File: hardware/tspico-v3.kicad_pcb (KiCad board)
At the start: 4 copper layers, 130 x 56 mm, 147 parts, among them J1 USB-C, J2 microSD, J3 OLED 1.27in 128x96, J4 3.5mm stereo, J5 Joystick, P1 TS2068_Edge, SW1 TS Reset, SW2 NMI, SW3 RUN, SW4 BOOTSEL, U1 74LVC245APW, U15 XL9555, U2 74LVC245APW, U20 RP2350B, U21 GD25Q128ESIGR, U22 APS6404L-3SQR-SN, U3 74LVC245APW, U30 TLV1117LV33, U31 TLV1117LV33, U4 74LVC245APW, U40 ESP32-C3-WROOM-02-N4, U50 MCP6002, U6 74LVC32APW, U7 74LVC06AD, Y1 12MHz

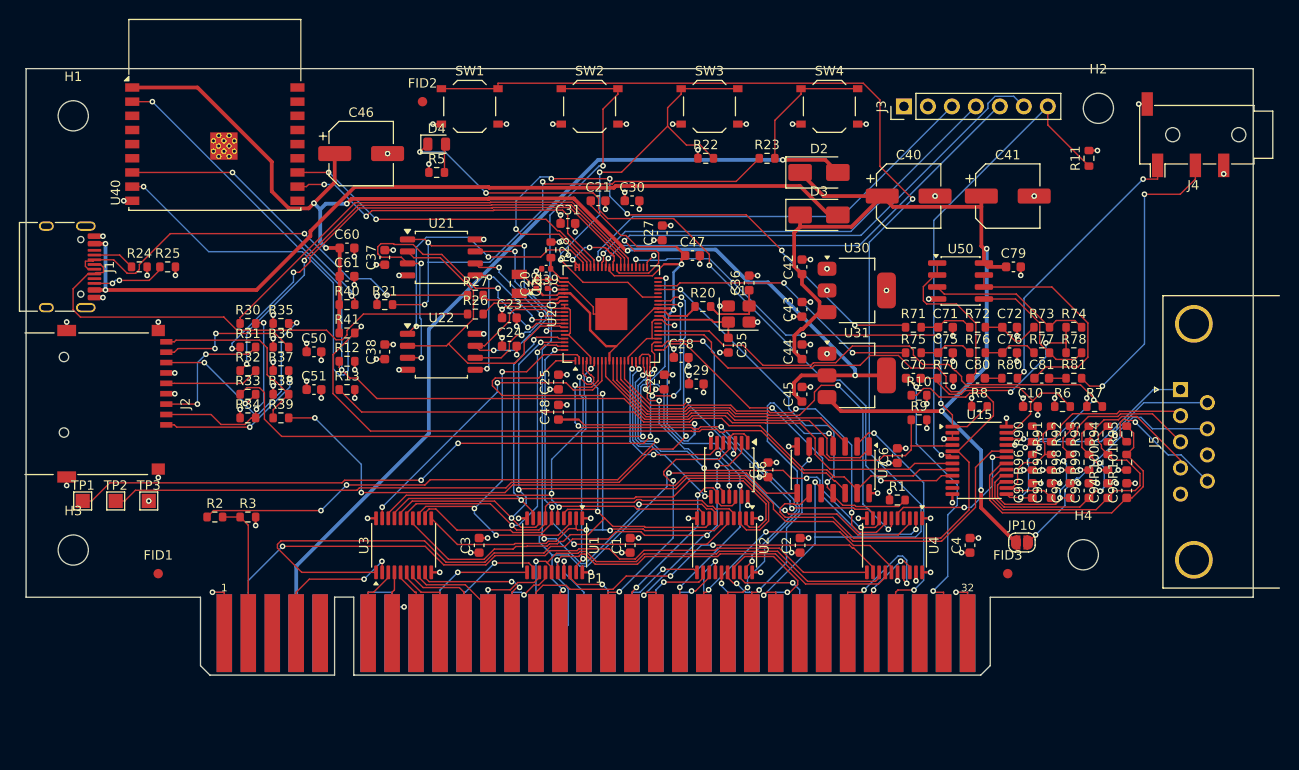
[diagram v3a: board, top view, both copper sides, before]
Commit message: Plain address bytes in hardware; DVDD spine and bottom-row fan pre-routed
U1 delivers A0-A7 and U2 A8-A15 on MD0-MD7 (U2 over its fingers, U1 in the row
above fed from both sides), so the firmware sees ordinary addresses. preroute.py
now also fixes the DVDD spine under the package, the inner 3.3 V supply links,
pin 51's capacitor and a deterministic fan for the fully used bottom pad row.
OLED_DC moves to GP34. Exposed pad gets five ground vias. finish.py: DVDD first,
clearance-aware widening, hairline fixes, unused-via cleanup, overlapping pads.
Fully routed, zero DRC errors; fab outputs regenerated.

Co-Authored-By: Claude Fable 5.1 <noreply@anthropic.com>
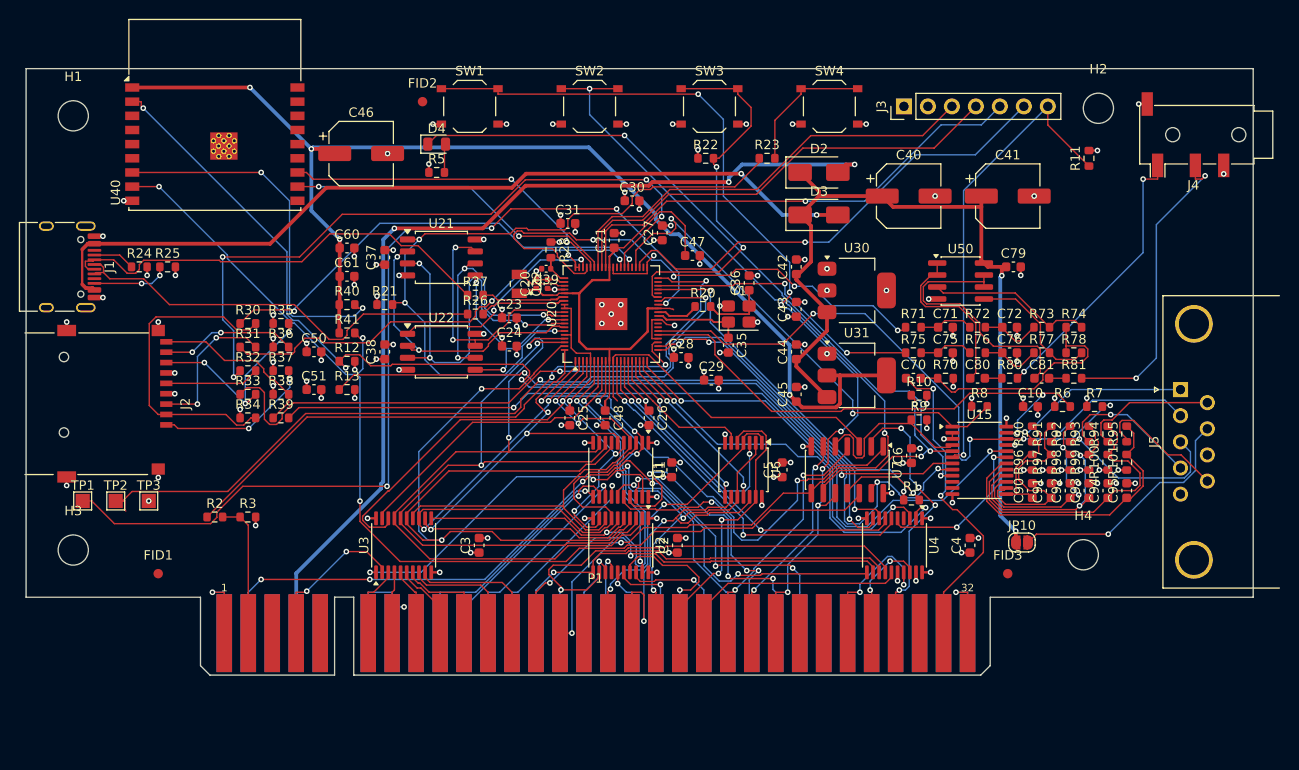
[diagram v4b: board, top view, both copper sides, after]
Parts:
- moved C2 13.0 mm to (69.0, 50.5)
- moved U2 11.0 mm to (63.0, 50.5)
- moved U1 10.6 mm to (63.0, 42.5)
- moved C1 9.13 mm to (68.4, 42.5)
- moved C48 4.99 mm to (61.4, 37.0), turned to -90 degrees
- moved C21 4.53 mm to (62.3, 18.2), turned to 90 degrees
- moved C26 4.12 mm to (66.0, 37.0), turned to -90 degrees
- moved C25 3.98 mm to (57.6, 37.0), turned to -90 degrees
- moved C29 1.65 mm to (72.6, 33.0)
- moved C5 1.50 mm to (80.1, 42.5)
- moved C6 1.50 mm to (93.8, 41.0)
- moved R1 1.50 mm to (93.8, 45.7)
- moved U6 1.50 mm to (76.0, 42.5)
- moved U7 1.50 mm to (87.0, 42.5)
- moved C42 0.60 mm to (81.6, 21.0)
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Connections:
- net nAEN_X renamed nAEN_LO
- net nAEN_Y renamed nAEN_HI
- U1 pad 15: /2068 Interface/A15 -> /2068 Interface/A7
- U1 pad 16: /2068 Interface/A14 -> /2068 Interface/A6
- U1 pad 17: /2068 Interface/A13 -> /2068 Interface/A5
- U1 pad 18: /2068 Interface/A12 -> /2068 Interface/A4
- U2 pad 11: /2068 Interface/A11 -> /2068 Interface/A15
- U2 pad 12: /2068 Interface/A10 -> /2068 Interface/A14
- U2 pad 13: /2068 Interface/A9 -> /2068 Interface/A13
- U2 pad 14: /2068 Interface/A8 -> /2068 Interface/A12
- U2 pad 15: /2068 Interface/A7 -> /2068 Interface/A11
- U2 pad 16: /2068 Interface/A6 -> /2068 Interface/A10
- U2 pad 17: /2068 Interface/A5 -> /2068 Interface/A9
- U2 pad 18: /2068 Interface/A4 -> /2068 Interface/A8
- U20 pad 43: unconnected-(U20-GPIO34-Pad43) -> OLED_DC
- U20 pad 49: OLED_DC -> unconnected-(U20-GPIO40/ADC0-Pad49)
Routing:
- net /2068 Interface/nRESET: track 132.0 -> 100.1 mm, vias 3 -> 7
- net /RP2350B Core/DVDD: track 83.4 -> 52.2 mm, vias 3 -> 0
- net NMI_REQ: track 50.7 -> 22.6 mm, vias 0 -> 3
- net MD2: track 63.4 -> 84.0 mm
- net +5V: track 108.9 -> 88.2 mm, vias 3 -> 2
- net /2068 Interface/A6: track 8.08 -> 27.9 mm, vias 1 -> 3
- net SD_SCK: track 54.3 -> 74.1 mm, vias 2 -> 4
- net nAEN_HI: track 45.7 -> 25.9 mm, vias 4 -> 2
- net /2068 Interface/A4: track 12.0 -> 31.5 mm, vias 1 -> 3
- net /2068 Interface/nRD: track 88.6 -> 69.7 mm, vias 4 -> 5
- net /RP2350B Core/SWCLK: track 82.0 -> 100.6 mm, vias 6 -> 4
- net /2068 Interface/A5: track 16.2 -> 34.8 mm, vias 1 -> 3
- net /2068 Interface/A7: track 6.72 -> 23.9 mm
- net /2068 Interface/nIORQ: track 24.0 -> 38.0 mm
- net /2068 Interface/nWAIT: track 39.1 -> 26.6 mm
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
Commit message: Board regenerated by the unattended flow: clean DRC with no hand edits
gen_layout -> preroute -> autoroute -> finish, run end to end. Fab outputs regenerated.

Co-Authored-By: Claude Fable 5.1 <noreply@anthropic.com>
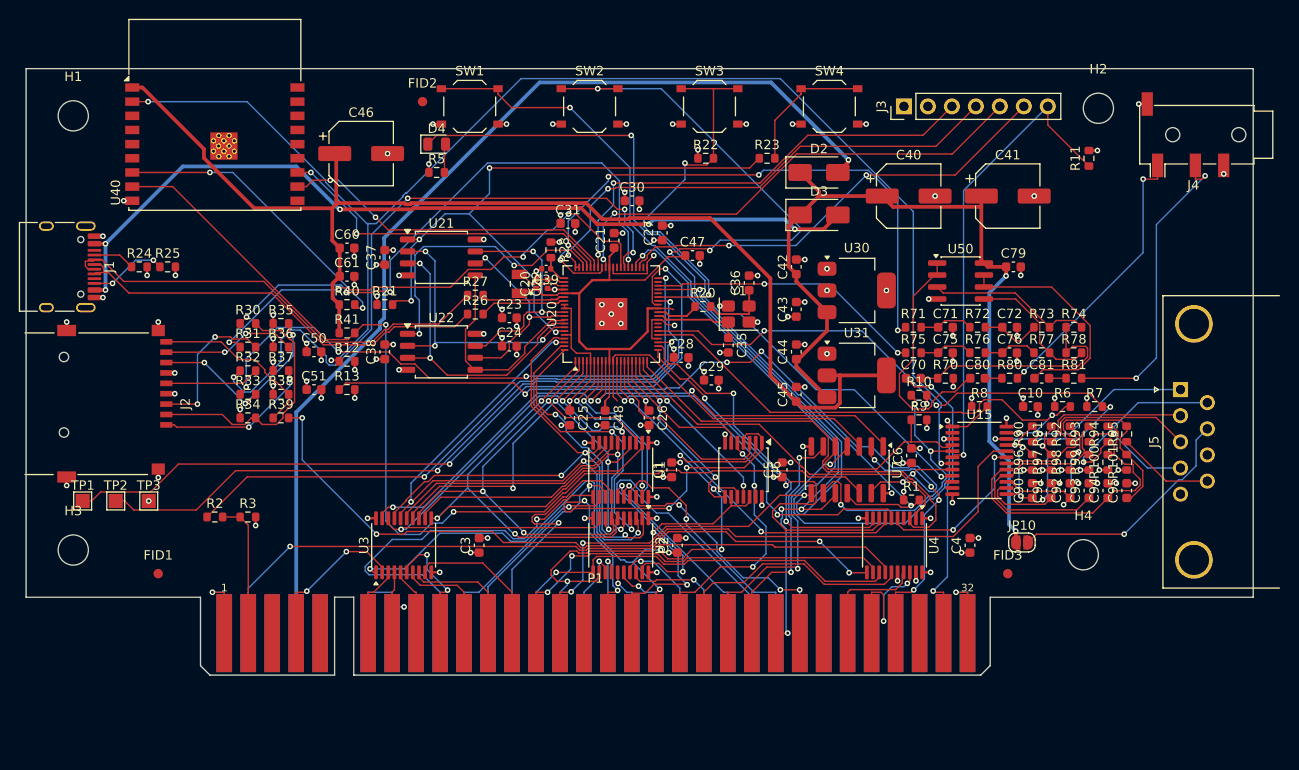
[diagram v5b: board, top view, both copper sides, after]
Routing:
- net WIFI_EN: track 113.2 -> 147.1 mm, vias 4 -> 3
- net MD2: track 84.0 -> 57.3 mm
- net /2068 Interface/nNMI: track 104.4 -> 126.3 mm, vias 4 -> 6
- net nIOX_INT: track 52.6 -> 72.0 mm
- net /2068 Interface/A0: track 25.2 -> 42.1 mm
- net MD0: track 75.5 -> 58.9 mm, vias 2 -> 3
- net /2068 Interface/nMREQ: track 32.0 -> 48.6 mm, vias 2 -> 4
- net /RP2350B Core/SWCLK: track 100.6 -> 85.2 mm, vias 4 -> 2
- net /2068 Interface/nRD: track 69.7 -> 84.5 mm, vias 5 -> 6
- net nAEN_HI: track 25.9 -> 39.6 mm
- net SD_CS: track 48.4 -> 60.4 mm, vias 2 -> 4
- net nINT_L: track 34.6 -> 44.2 mm
- net MD5: track 64.6 -> 55.1 mm, vias 2 -> 3
- net BE_REQ: track 47.4 -> 38.0 mm
- net OLED_SCK: track 48.9 -> 57.9 mm, vias 0 -> 2
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
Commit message: Silkscreen pass: designators placed clear of pads and edge; DRC clean at every severity
silk.py places 103 of 140 reference designators at 0.8 mm, hides the ones in
rows too dense to label (still on F.Fab), and trims connector outlines at the
board edge. finish.py now peels back the stubs left by removed unused vias.

Co-Authored-By: Claude Fable 5.1 <noreply@anthropic.com>
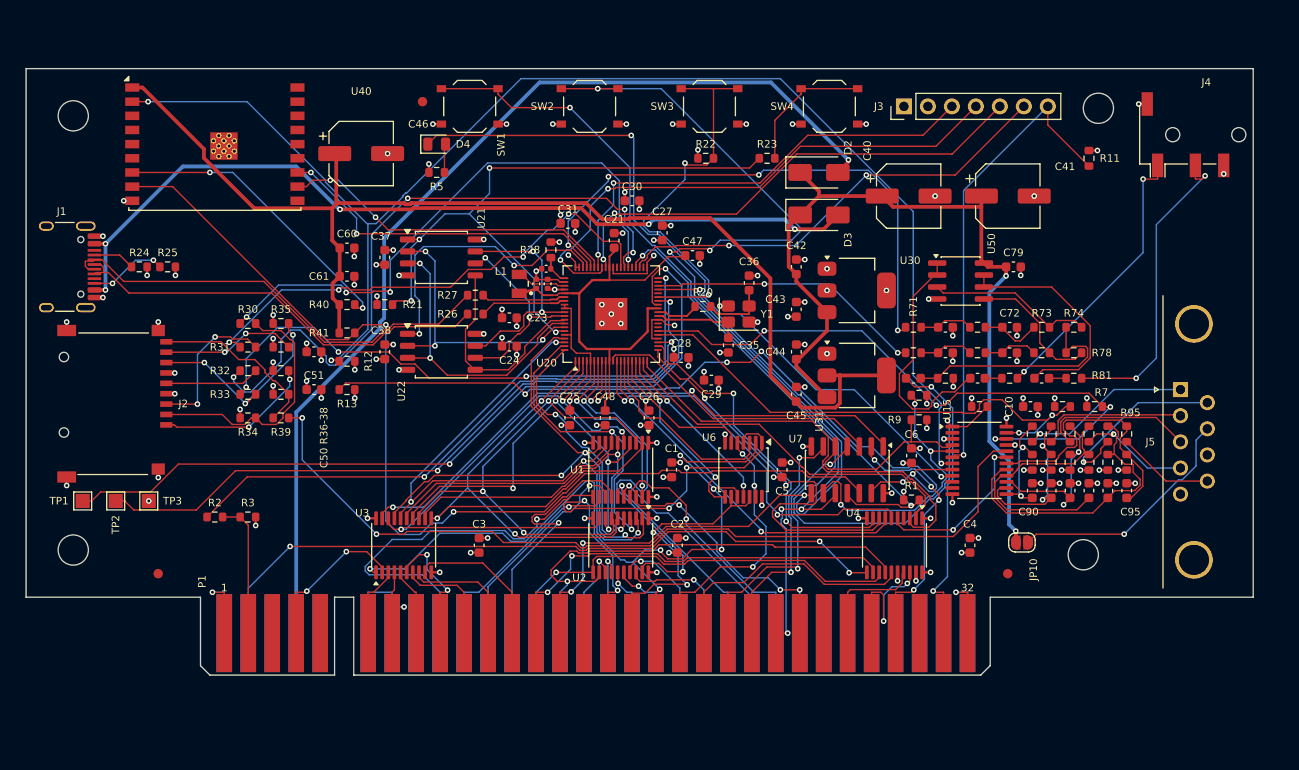
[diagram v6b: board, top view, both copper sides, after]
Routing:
- net WAIT_REQ: track 35.2 -> 30.7 mm
- net /RP2350B Core/DVDD: track 48.4 -> 46.7 mm
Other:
- board text added: "C50 R36-38"

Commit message: Respace audio, joystick and SD passives for silkscreen; rerouted, DRC clean
Rows and columns of passives now leave room for a designator beside each part:
139 of 140 are on silk (only C39 in the regulator cluster is hidden). silk.py
sizes labels by their glyphs, keeps a row's labels on one side and retries hidden
ones by moving a neighbour. finish.py peels unused stubs in fresh interpreters
and fetches zones before removals (pcbnew segfaulted otherwise).

Co-Authored-By: Claude Fable 5.1 <noreply@anthropic.com>
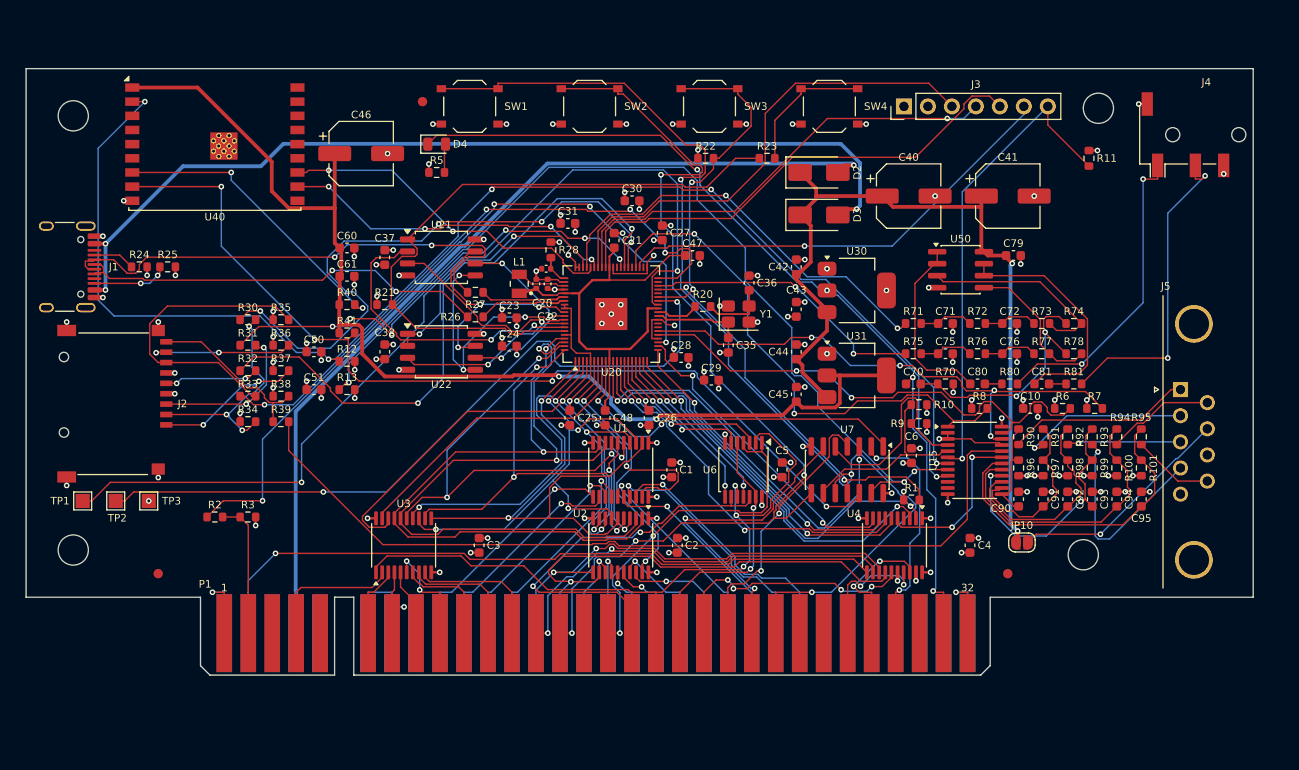
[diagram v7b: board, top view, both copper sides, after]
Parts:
- moved C95 1.79 mm to (118.2, 45.6)
- moved C90 1.71 mm to (105.2, 45.6)
- moved R101 1.66 mm to (118.2, 42.3)
- moved R95 1.58 mm to (118.2, 39.0)
- moved R96 1.57 mm to (105.2, 42.3)
- moved R90 1.48 mm to (105.2, 39.0)
- moved C94 1.31 mm to (115.5, 45.6)
- moved C91 1.24 mm to (107.8, 45.6)
- moved C79 1.20 mm to (104.6, 19.8)
- moved U50 1.20 mm to (99.0, 21.3)
- moved R100 1.12 mm to (115.5, 42.3)
- moved R97 1.04 mm to (107.8, 42.3)
- moved R10 1.00 mm to (94.6, 35.6)
- moved R94 1.00 mm to (115.5, 39.0)
- moved C93 0.97 mm to (113.0, 45.6)
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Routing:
- net /2068 Interface/nRESET: track 92.2 -> 115.3 mm, vias 4 -> 3
- net /2068 Interface/nNMI: track 126.3 -> 103.7 mm, vias 6 -> 4
- net TAPE_OUT: track 59.6 -> 78.2 mm, vias 2 -> 4
- net /2068 Interface/A0: track 42.1 -> 25.4 mm
- net nIOX_INT: track 72.0 -> 55.9 mm
- net WIFI_DL: track 85.5 -> 100.8 mm, vias 5 -> 3
- net AUDIO_L: track 59.3 -> 44.8 mm, vias 4 -> 2
- net WAIT_REQ: track 30.7 -> 43.6 mm, vias 0 -> 2
- net /RP2350B Core/SWCLK: track 85.2 -> 97.7 mm
- net /2068 Interface/nMREQ: track 48.6 -> 36.9 mm, vias 4 -> 2
- net /2068 Interface/nIORQ: track 30.7 -> 42.3 mm
- net nAEN_HI: track 39.6 -> 28.3 mm
- net +5V_EDGE: track 106.9 -> 95.6 mm
- net MD3: track 60.9 -> 49.9 mm, vias 3 -> 4
- net I2C_SCL: track 68.3 -> 57.7 mm
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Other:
- board text removed: "C50 R36-38"
